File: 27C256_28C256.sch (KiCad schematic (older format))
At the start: 3 parts, among them J1 27C256 DIP LEGS, U1 28C256

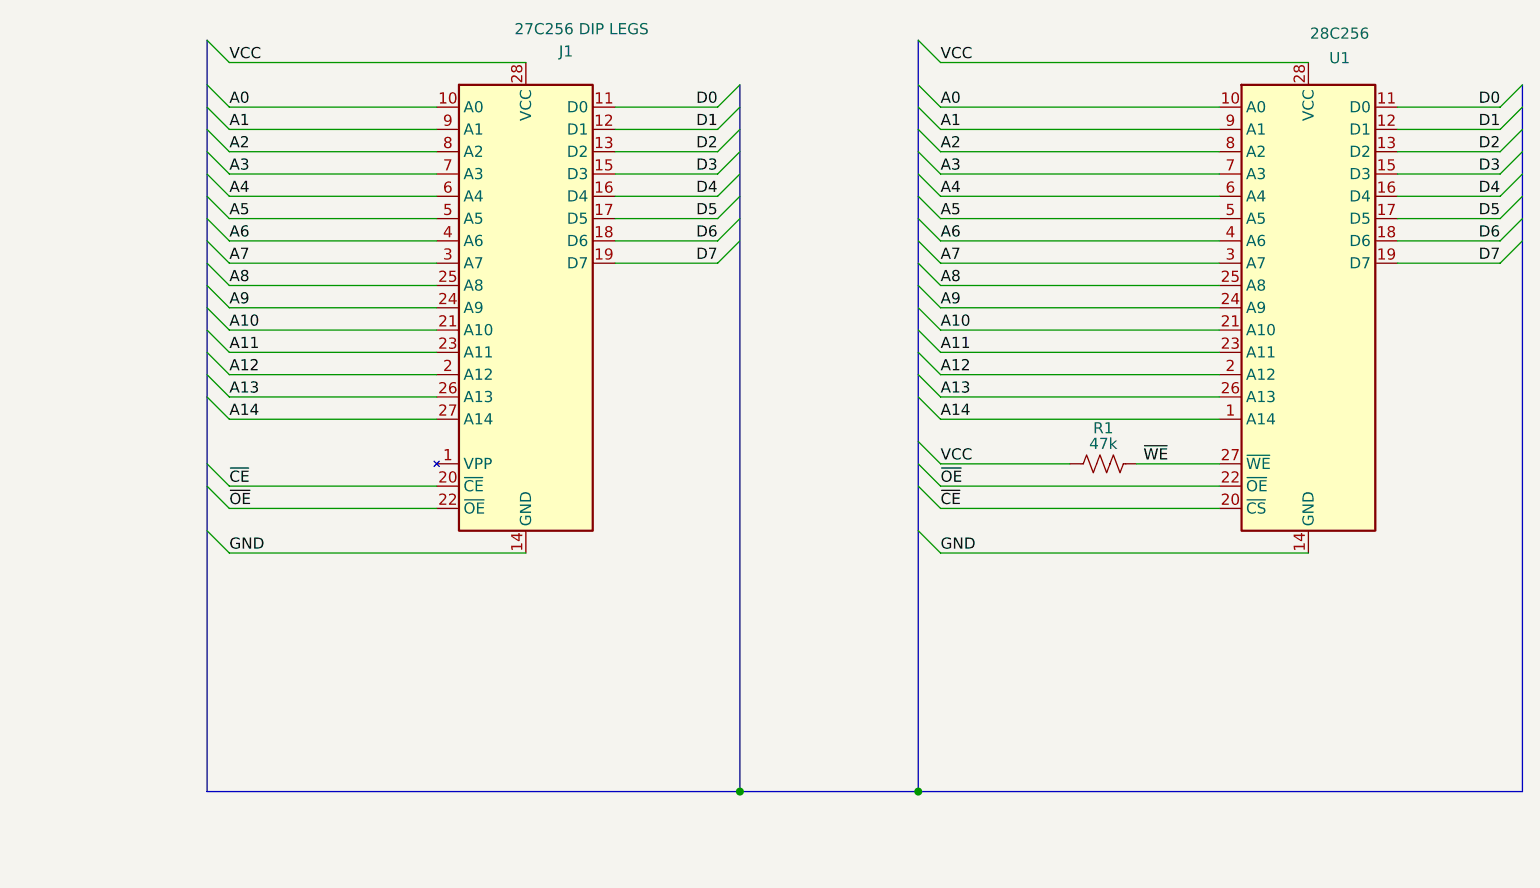
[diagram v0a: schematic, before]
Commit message: 27C256_28C256: add jumpers to allow programming without needing a test clip
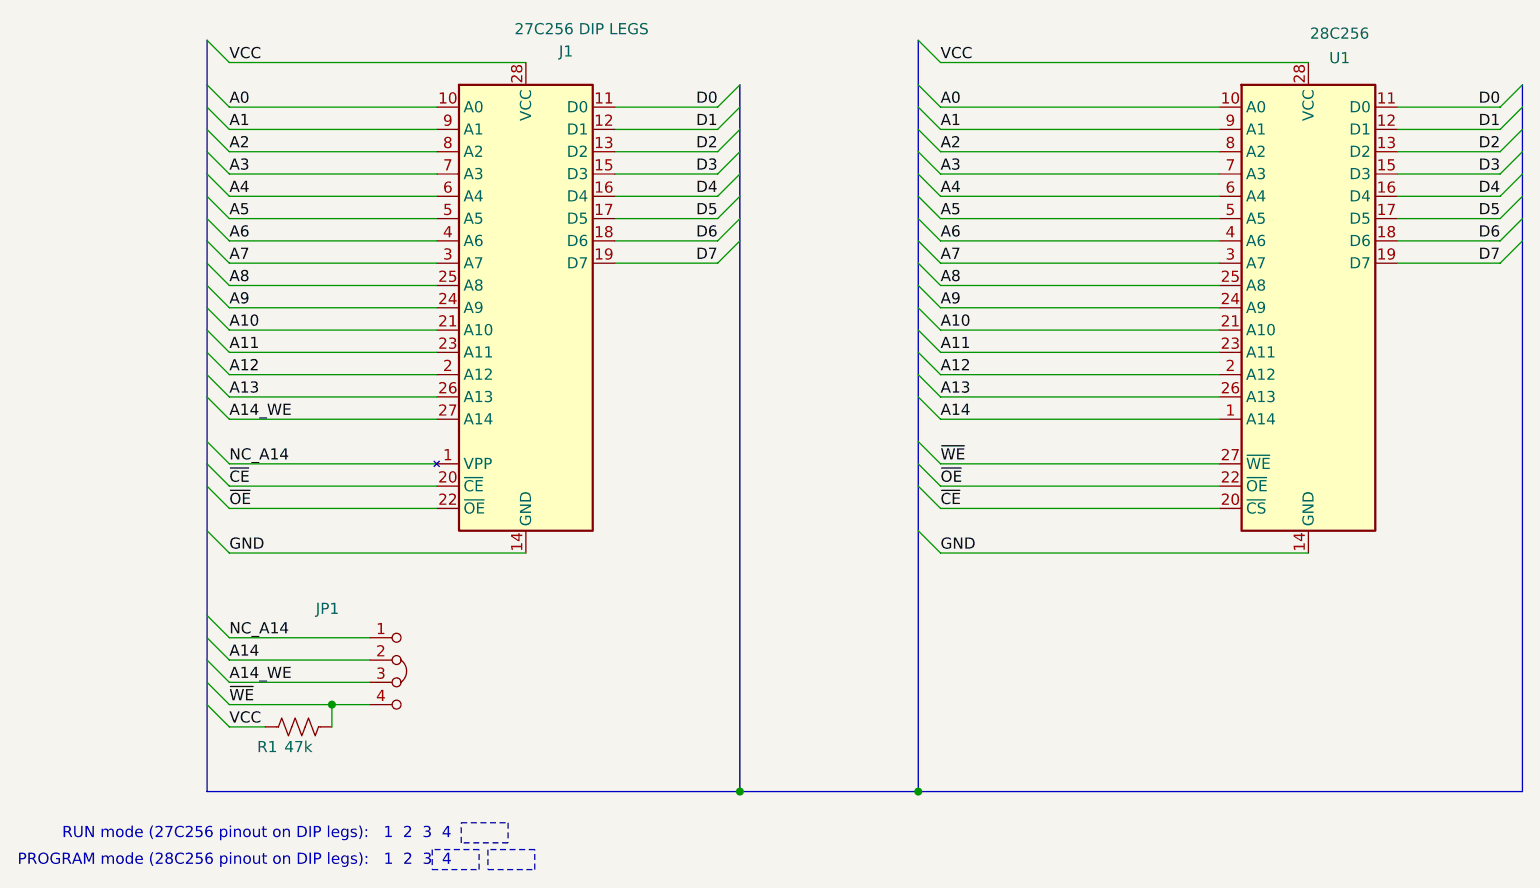
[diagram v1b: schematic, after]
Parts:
- added JP1: Jumper_3_Bridged12, 000_LOCAL:Pin_Header_Angled_1x04_Pitch2.54mm, symbol 000_LOCAL:Jumper_4_Bridged23
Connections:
- net A14: now also JP1.2 (B); no longer J1.27 (A14)
- net ~WE: now also JP1.4 (D)
- net NC_A14: now reaches J1.1 (VPP)
- net NC_A14: now also JP1.1 (A)
- new net A14_WE: J1.27 (A14), JP1.3 (C)
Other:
- note added: "PROGRAM mode (28C256 pinout on DIP legs): 1 2 3 4"
- note added: "RUN mode (27C256 pinout on DIP legs): 1 2 3 4"
- moved on the sheet: R1
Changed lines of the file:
@@
 	1    0    0    -1
 $EndComp
-$Comp
-L 000_LOCAL:R_US R1
-U 1 1 5E5D421C
-P 6630 4250
-F 0 "R1" V 6470 4250 50  0000 C CNN
-F 1 "47k" V 6540 4250 50  0000 C CNN
-F 2 "000_LOCAL:R_0805" V 6670 4240 50  0001 C CNN
-F 3 "~" H 6630 4250 50  0001 C CNN
-	1    6630 4250
-	0    1    1    0
-$EndComp
-Wire Wire Line
-	7150 4250 6780 4250
 Entry Wire Line
 	5800 2550 5900 2650
-Wire Bus Line
-	5800 5720 5000 5720
 Entry Wire Line
 	2610 2550 2710 2650
@@
 Entry Wire Line
 	5800 2350 5900 2450
-Wire Wire Line
-	6480 4250 5900 4250
-Entry Wire Line
-	5800 4150 5900 4250
-Wire Wire Line
-	7550 4650 5900 4650
-Entry Wire Line
-	5800 4550 5900 4650
 Wire Wire Line
 	5900 2650 7150 2650
@@
 VCC
 Text Label 5900 4250 0    50   ~ 0
-VCC
-Text Label 6810 4250 0    50   ~ 0
 ~WE
-Text Label 5900 4650 0    50   ~ 0
-GND
-Entry Wire Line
-	5800 4250 5900 4350
-Wire Wire Line
-	5900 4350 7150 4350
-Entry Wire Line
-	5800 4350 5900 4450
-Wire Wire Line
-	5900 4450 7150 4450
 Wire Wire Line
 	4040 2450 2710 2450
@@
 Text Label 2710 4450 0    50   ~ 0
 ~OE
-Text Label 5900 4350 0    50   ~ 0
-~OE
-Text Label 5900 4450 0    50   ~ 0
-~CE
 Text Label 2710 2750 0    50   ~ 0
 A1
@@
 A13
 Text Label 2710 4050 0    50   ~ 0
-A14
+A14_WE
 Text Label 5900 2650 0    50   ~ 0
 A0
@@
 Text Label 8410 3350 2    50   ~ 0
 D7
+$Comp
+L 000_LOCAL:Jumper_4_Bridged23 JP1
+U 1 1 5E638C0C
+P 3590 5030
+F 0 "JP1" H 3150 5160 50  0000 C CNN
+F 1 "Jumper_3_Bridged12" H 4360 4920 50  0001 C CNN
+F 2 "000_LOCAL:Pin_Header_Angled_1x04_Pitch2.54mm" H 3590 5030 50  0001 C CNN
+F 3 "~" H 3590 5030 50  0001 C CNN
+	1    3590 5030
+	1    0    0    -1
+$EndComp
+Entry Wire Line
+	2610 5130 2710 5230
+Entry Wire Line
+	2610 5230 2710 5330
+Entry Wire Line
+	2610 5030 2710 5130
+Text Label 2710 5230 0    50   ~ 0
+A14_WE
+Text Label 2710 5130 0    50   ~ 0
+A14
+Text Label 2710 5330 0    50   ~ 0
+~WE
+Connection ~ 5800 5720
 Wire Bus Line
 	8510 5720 5800 5720
-Connection ~ 5800 5720
+Wire Bus Line
+	5800 5720 5000 5720
+Text Label 5900 4450 0    50   ~ 0
+~CE
+Text Label 5900 4350 0    50   ~ 0
+~OE
+Wire Wire Line
+	5900 4450 7150 4450
+Entry Wire Line
+	5800 4350 5900 4450
+Wire Wire Line
+	5900 4350 7150 4350
+Entry Wire Line
+	5800 4250 5900 4350
+Text Label 5900 4650 0    50   ~ 0
+GND
+Text Label 2710 5430 0    50   ~ 0
+VCC
+Entry Wire Line
+	5800 4550 5900 4650
+Wire Wire Line
+	7550 4650 5900 4650
+Entry Wire Line
+	5800 4150 5900 4250
+$Comp
+L 000_LOCAL:R_US R1
+U 1 1 5E5D421C
+P 3020 5430
+F 0 "R1" V 3110 5290 50  0000 C CNN
+F 1 "47k" V 3110 5430 50  0000 C CNN
+F 2 "000_LOCAL:R_0805" V 3060 5420 50  0001 C CNN
+F 3 "~" H 3020 5430 50  0001 C CNN
+	1    3020 5430
+	0    1    1    0
+$EndComp
+Entry Wire Line
+	2610 5330 2710 5430
+Wire Wire Line
+	2710 5430 2870 5430
+Wire Wire Line
+	5900 4250 7150 4250
+Entry Wire Line
+	2610 4930 2710 5030
+Entry Wire Line
+	2610 4150 2710 4250
+Wire Wire Line
+	2710 4250 3640 4250
+Text Label 2710 4250 0    50   ~ 0
+NC_A14
+Text Label 2710 5030 0    50   ~ 0
+NC_A14
+Wire Wire Line
+	3170 5330 2710 5330
+Wire Wire Line
+	3170 5330 3170 5430
+Wire Wire Line
+	2710 5030 3340 5030
+Wire Wire Line
+	2710 5130 3340 5130
+Wire Wire Line
+	2710 5230 3340 5230
+Wire Wire Line
+	3170 5330 3340 5330
+Connection ~ 3170 5330
+Text Notes 1960 5940 0    50   ~ 0
+RUN mode (27C256 pinout on DIP legs):   1  2  3  4
+Text Notes 1760 6060 0    50   ~ 0
+PROGRAM mode (28C256 pinout on DIP legs):   1  2  3  4
+Wire Notes Line style solid
+	3830 5980 3620 5980
+Wire Notes Line style solid
+	3620 5980 3620 6070
+Wire Notes Line style solid
+	3620 6070 3830 6070
+Wire Notes Line style solid
+	3830 6070 3830 5980
+Wire Notes Line style solid
+	3870 5980 3870 6070
+Wire Notes Line style solid
+	3870 6070 4080 6070
+Wire Notes Line style solid
+	4080 6070 4080 5980
+Wire Notes Line style solid
+	4080 5980 3870 5980
+Wire Notes Line style solid
+	3750 5950 3750 5860
+Wire Notes Line style solid
+	3750 5860 3960 5860
+Wire Notes Line style solid
+	3960 5860 3960 5950
+Wire Notes Line style solid
+	3960 5950 3750 5950
+Wire Bus Line
+	8510 2550 8510 5720
 Wire Bus Line
 	5000 2550 5000 5720
 Wire Bus Line
-	8510 2550 8510 5720
-Wire Bus Line
 	2610 2350 2610 5720

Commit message: footprint name changed
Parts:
- J1: footprint 000_LOCAL:DIP-28_W15.24mm_pcb_sil_pins -> 000_LOCAL:DIP28_0.6_pcb_sil_pins
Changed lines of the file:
@@
 F 0 "J1" H 4220 4700 50  0000 C CNN
 F 1 "27C256 DIP LEGS" H 4290 4800 50  0000 C CNN
-F 2 "000_LOCAL:DIP-28_W15.24mm_pcb_sil_pins" H 4040 3550 50  0001 C CNN
+F 2 "000_LOCAL:DIP28_0.6_pcb_sil_pins" H 4040 3550 50  0001 C CNN
 F 3 "http://ww1.microchip.com/downloads/en/DeviceDoc/doc0014.pdf" H 4040 3550 50  0001 C CNN
 	1    4040 3550
